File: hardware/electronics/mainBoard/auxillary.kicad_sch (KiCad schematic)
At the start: 28 parts, among them J10 M.2 Standoff, J11 M.2 Standoff, J9 Bus_M.2_Socket_E, SW7 JS102011JCQN, SW8 JS102011JCQN, U13 TPS22996H-Q1, U14 TXS0108EQWRKSRQ1, U15 TXS0104VxRUTR

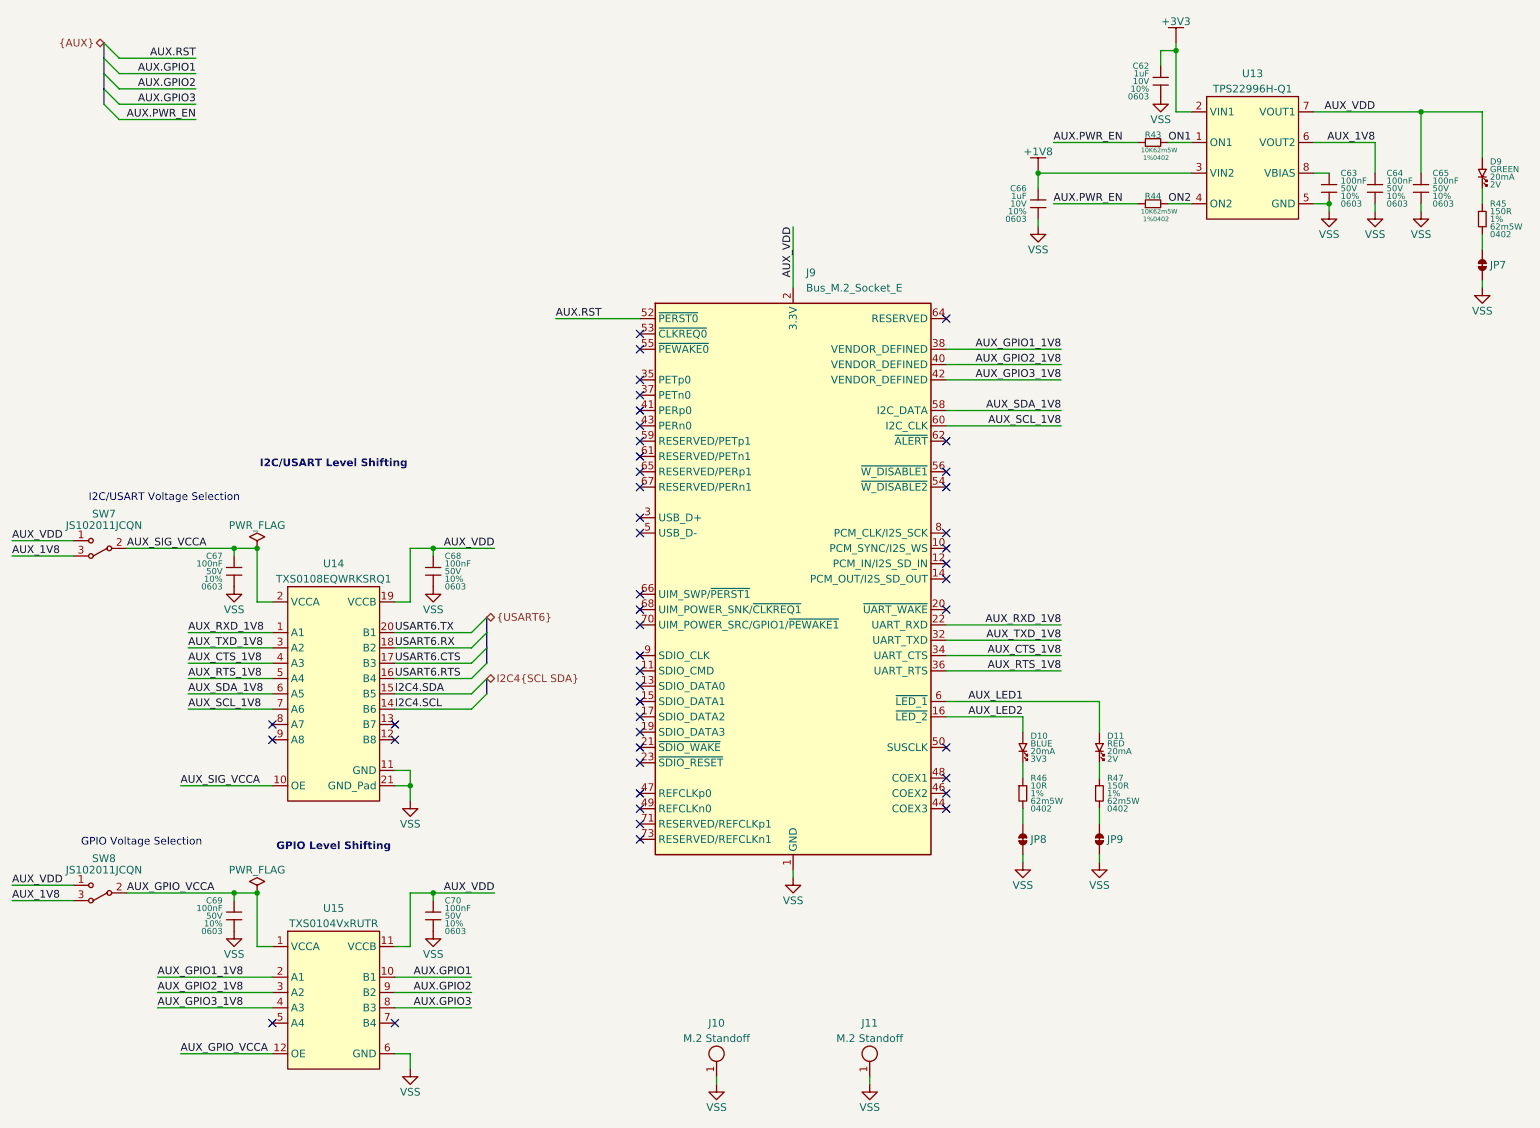
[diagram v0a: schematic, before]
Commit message: updated capacitors
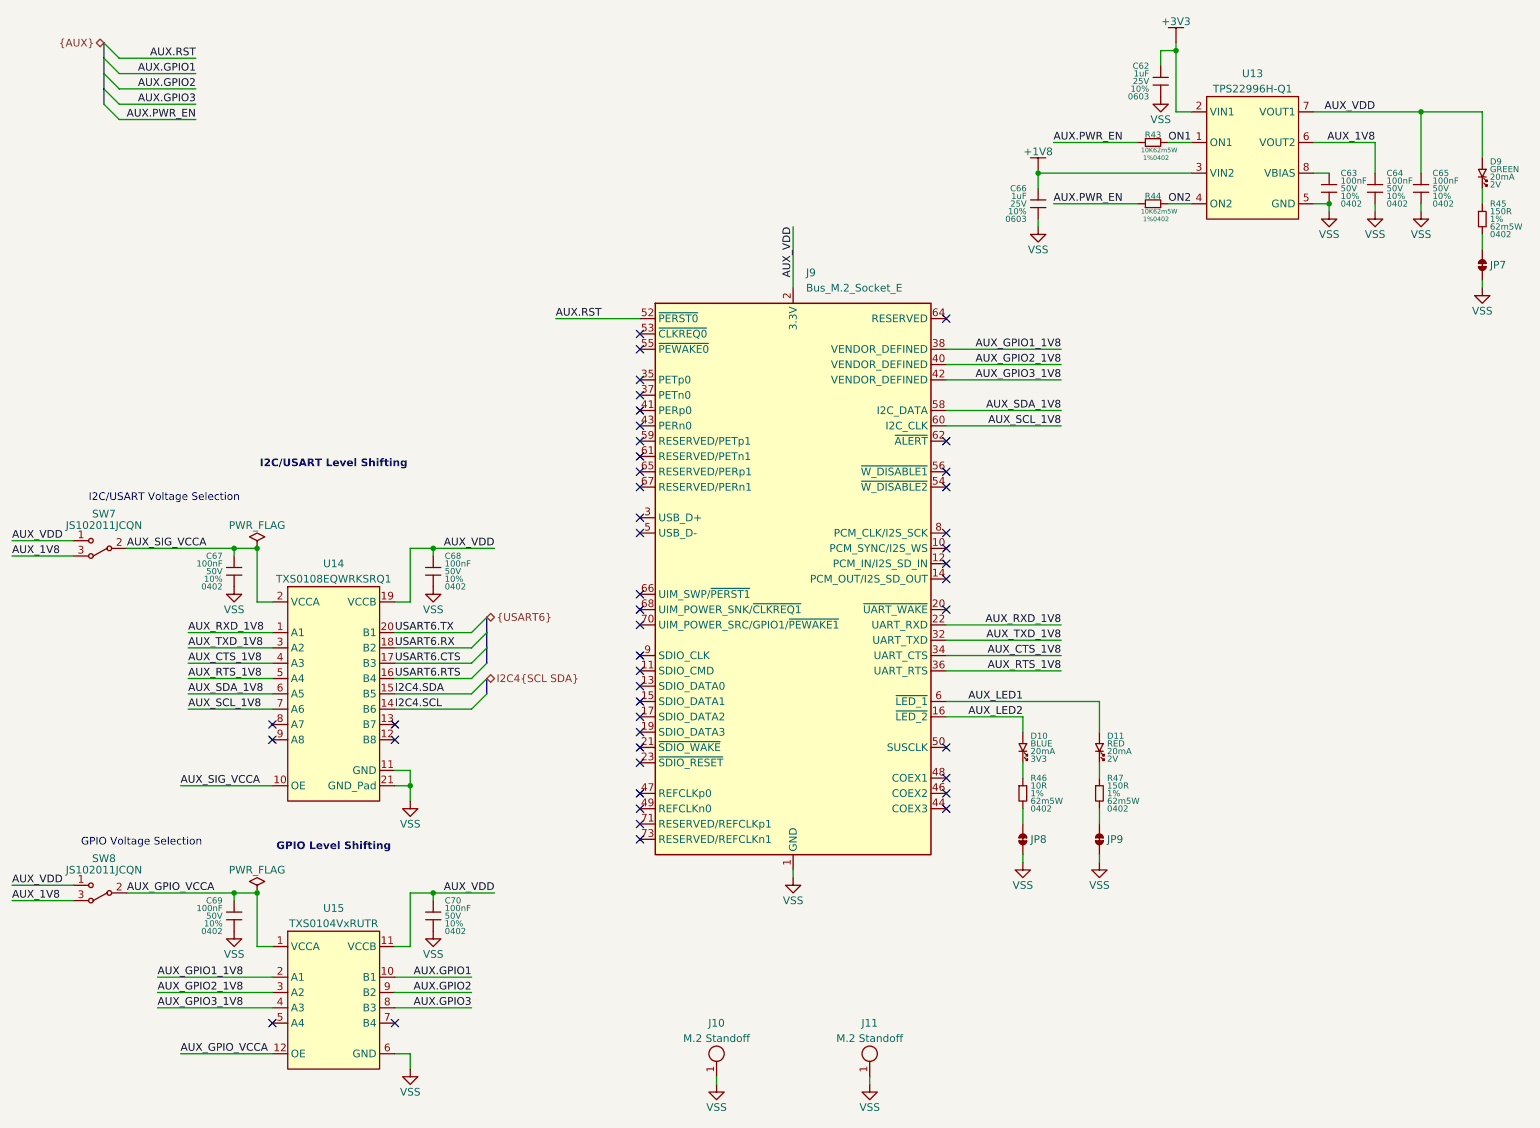
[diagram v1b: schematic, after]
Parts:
- C62, C66: DKPN 478-KAM15AR71A105KTCT-ND -> 490-GRT188R71E105KE13DCT-ND; MPN KAM15AR71A105KT -> GRT188R71E105KE13D; Manufacturer KYOCERA AVX -> Murata Electronics; Voltage Rating 10V -> 25V
- C63, C64, C65, C67, C68, C69, C70: DKPN 478-KAM15AR71H104KTCT-ND -> 490-GRT155R71H104KE01DCT-ND; MPN 06035C104K4T2A -> GRT155R71H104KE01D; Manufacturer KYOCERA AVX -> Murata Electronics; Package 0603 -> 0402

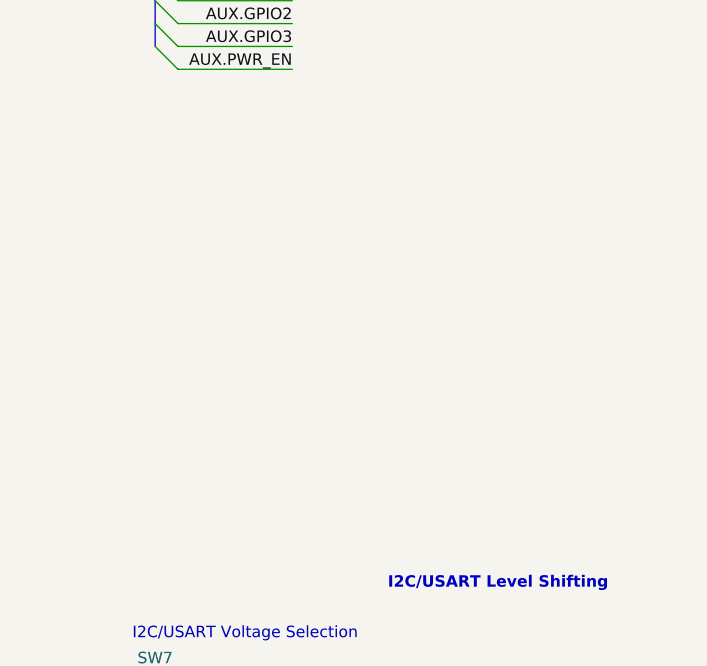
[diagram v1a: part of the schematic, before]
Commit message: added testpoints
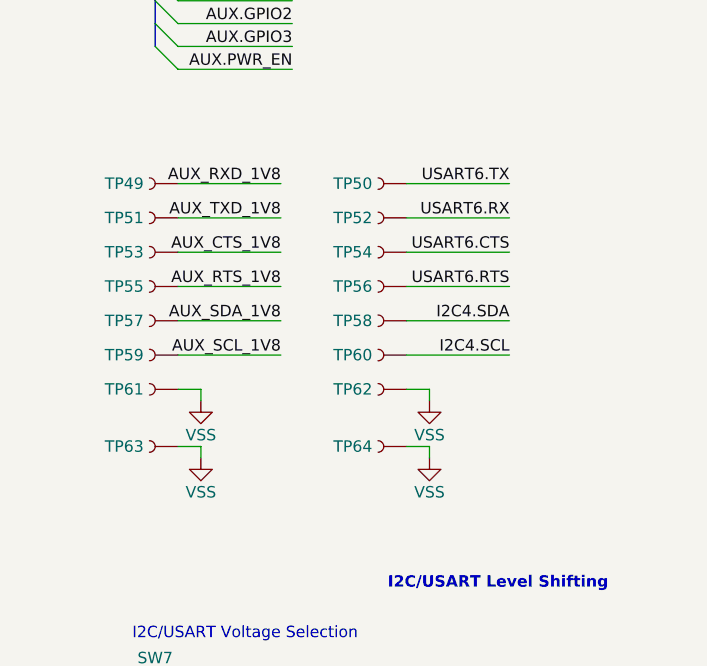
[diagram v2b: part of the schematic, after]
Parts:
- added TP49, TP50, TP51, TP52, TP53, TP54, TP55, TP56, TP57, TP58, TP59, TP60: ~, symbol lib_sch:Testpoint
- added TP61, TP62, TP63, TP64: RCWCTE, symbol lib_sch:Testpoint
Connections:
- net AUX_CTS_1V8: now also TP53.1
- net AUX_RTS_1V8: now also TP55.1
- net AUX_RXD_1V8: now also TP49.1
- net AUX_SCL_1V8: now also TP59.1
- net AUX_SDA_1V8: now also TP57.1
- net AUX_TXD_1V8: now also TP51.1
- net I2C4.SCL: now also TP60.1
- net I2C4.SDA: now also TP58.1
- net USART6.CTS: now also TP54.1
- net USART6.RTS: now also TP56.1
- net USART6.RX: now also TP52.1
- net USART6.TX: now also TP50.1
- net VSS: now also TP61.1, TP62.1, TP63.1, TP64.1

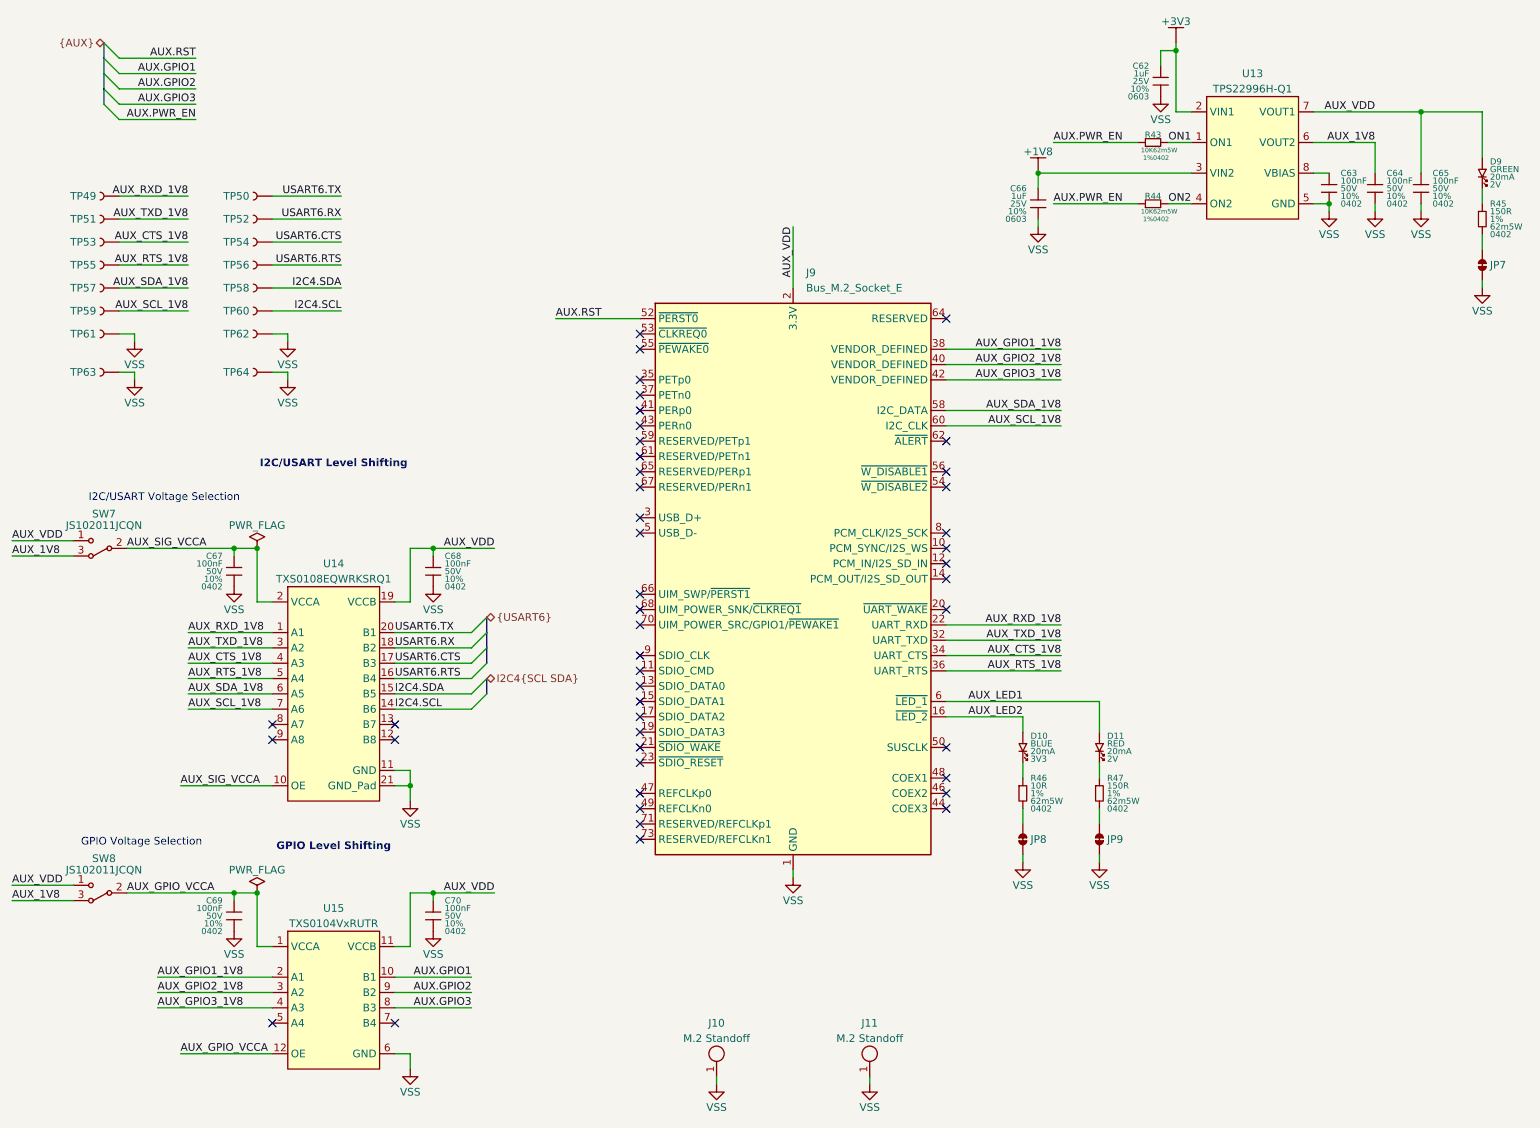
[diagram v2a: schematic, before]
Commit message: updated symbol refs
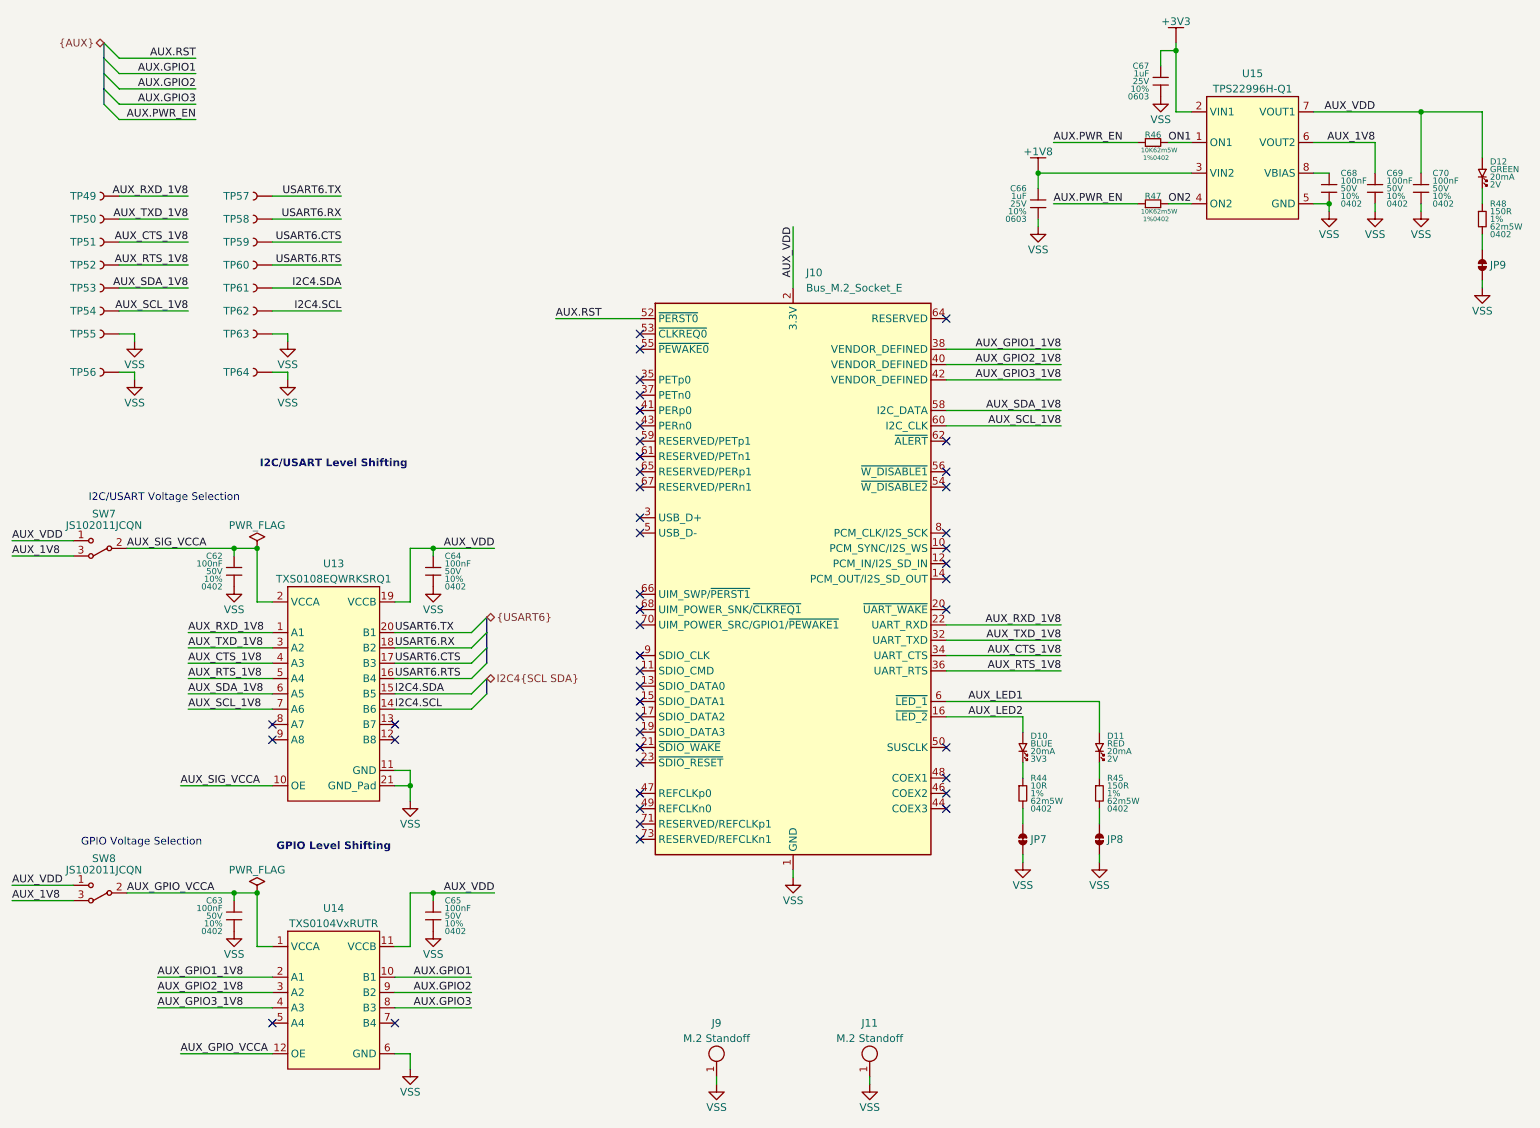
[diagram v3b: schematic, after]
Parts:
- renumbered C67 to C62, C69 to C63, C68 to C64, C70 to C65, C62 to C67, C63 to C68, C64 to C69, C65 to C70, D9 to D12, J9 to J10, J10 to J9, JP8 to JP7, JP9 to JP8, JP7 to JP9, R46 to R44, R47 to R45, R43 to R46, R44 to R47, R45 to R48, TP51 to TP50, TP53 to TP51, TP55 to TP52, TP57 to TP53, TP59 to TP54, TP61 to TP55, TP63 to TP56, TP50 to TP57, TP52 to TP58, TP54 to TP59, TP56 to TP60, TP58 to TP61, TP60 to TP62, TP62 to TP63, U14 to U13, U15 to U14, U13 to U15

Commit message: updated symbol refs
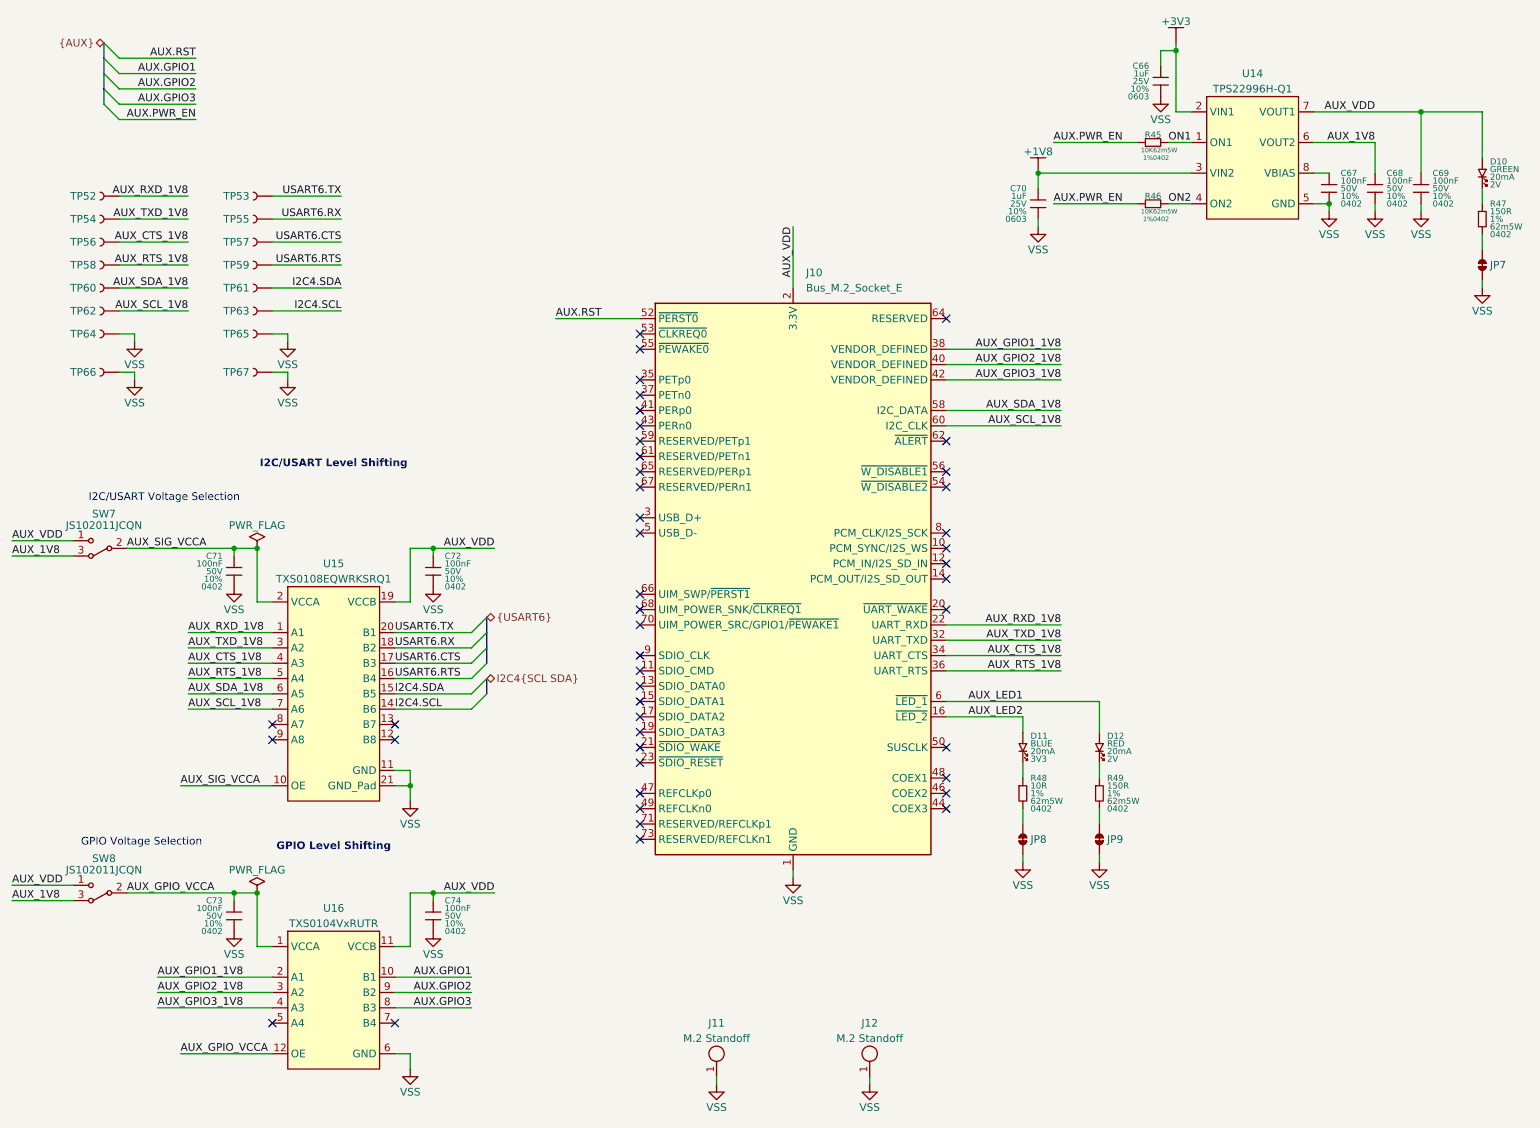
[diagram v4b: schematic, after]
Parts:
- renumbered C67 to C66, C68 to C67, C69 to C68, C70 to C69, C66 to C70, C62 to C71, C64 to C72, C63 to C73, C65 to C74, D12 to D10, D10 to D11, D11 to D12, J9 to J11, J11 to J12, JP9 to JP7, JP7 to JP8, JP8 to JP9, R46 to R45, R47 to R46, R48 to R47, R44 to R48, R45 to R49, TP49 to TP52, TP57 to TP53, TP50 to TP54, TP58 to TP55, TP51 to TP56, TP59 to TP57, TP52 to TP58, TP60 to TP59, TP53 to TP60, TP54 to TP62, TP62 to TP63, TP55 to TP64, TP63 to TP65, TP56 to TP66, TP64 to TP67, U15 to U14, U13 to U15, U14 to U16

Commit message: assigned FPs
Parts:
- J10: footprint (none) -> lib_connectors:MDT420E01001
- SW7, SW8: footprint (none) -> lib_switches:JS102011JCQN
- U14: footprint (none) -> lib_ICs:SOT583
- U16: footprint (none) -> lib_ICs:QFN40P170X200X55-12
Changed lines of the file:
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@@
 			)
 		)
-		(property "Footprint" ""
+		(property "Footprint" "lib_ICs:QFN40P170X200X55-12"
 			(at 63.5 181.61 0)
 			(effects
@@
 			)
 		)
-		(property "Footprint" ""
+		(property "Footprint" "lib_switches:JS102011JCQN"
 			(at 25.4 102.87 0)
 			(effects
@@
 			)
 		)
-		(property "Footprint" ""
+		(property "Footprint" "lib_connectors:MDT420E01001"
 			(at 139.7 81.28 0)
 			(effects
@@
 			)
 		)
-		(property "Footprint" ""
+		(property "Footprint" "lib_ICs:SOT583"
 			(at 215.9 38.1 0)
 			(effects
@@
 			)
 		)
-		(property "Footprint" ""
+		(property "Footprint" "lib_switches:JS102011JCQN"
 			(at 25.4 160.02 0)
 			(effects
